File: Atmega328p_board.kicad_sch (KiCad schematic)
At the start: 25 parts, among them U1 24LC1025, U2 24LC1025, U3 ATMEGA328P-AU, U4 DS1337S_, Y1 16MHz, Y2 32.768 KHz

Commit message: Completed commits
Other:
- note added: "EEPROM"
- note added: "MCU"
- note added: "Mounting"
- note added: "RTC"
- moved on the sheet: H1, H2, H3, H4

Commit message: Routing completed.
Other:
- title: (none) -> MCU Datalogger with EEPROM and RTC
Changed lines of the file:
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@@
 (kicad_sch (version 20230121) (generator eeschema)
   (paper "A4")
+  (title_block
+    (title "MCU Datalogger with EEPROM and RTC")
+  )
   (junction (at 164.465 60.325) (diameter 0) (color 0 0 0 0)
   )

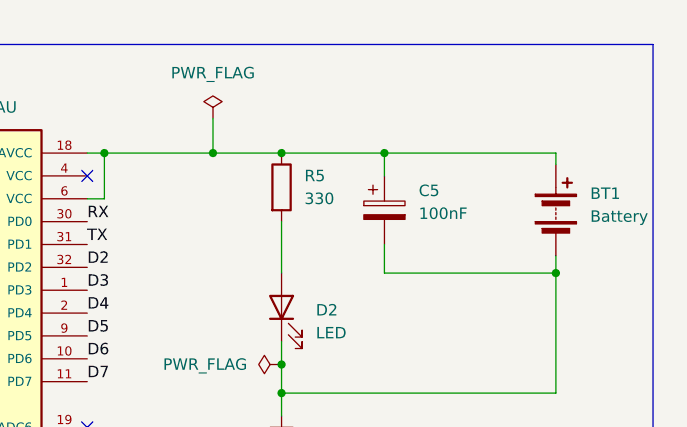
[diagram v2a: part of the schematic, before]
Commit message: COmpleted with silkscreen and footprints(logo).
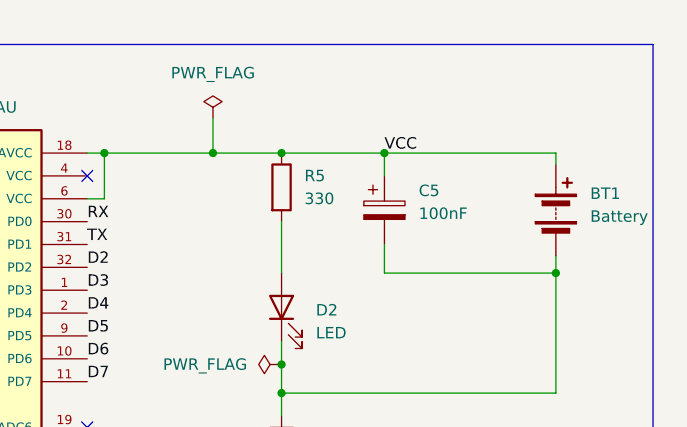
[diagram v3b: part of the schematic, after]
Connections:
- net VCC: now also BT1.1 (+), C5.1, R5.1, U3.18 (AVCC), U3.6 (VCC)
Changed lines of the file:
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@@
+    (effects (font (size 1.27 1.27)) (justify left bottom))
+  )
+  (label "VCC" (at 248.92 31.75 0) (fields_autoplaced)
     (effects (font (size 1.27 1.27)) (justify left bottom))
   )

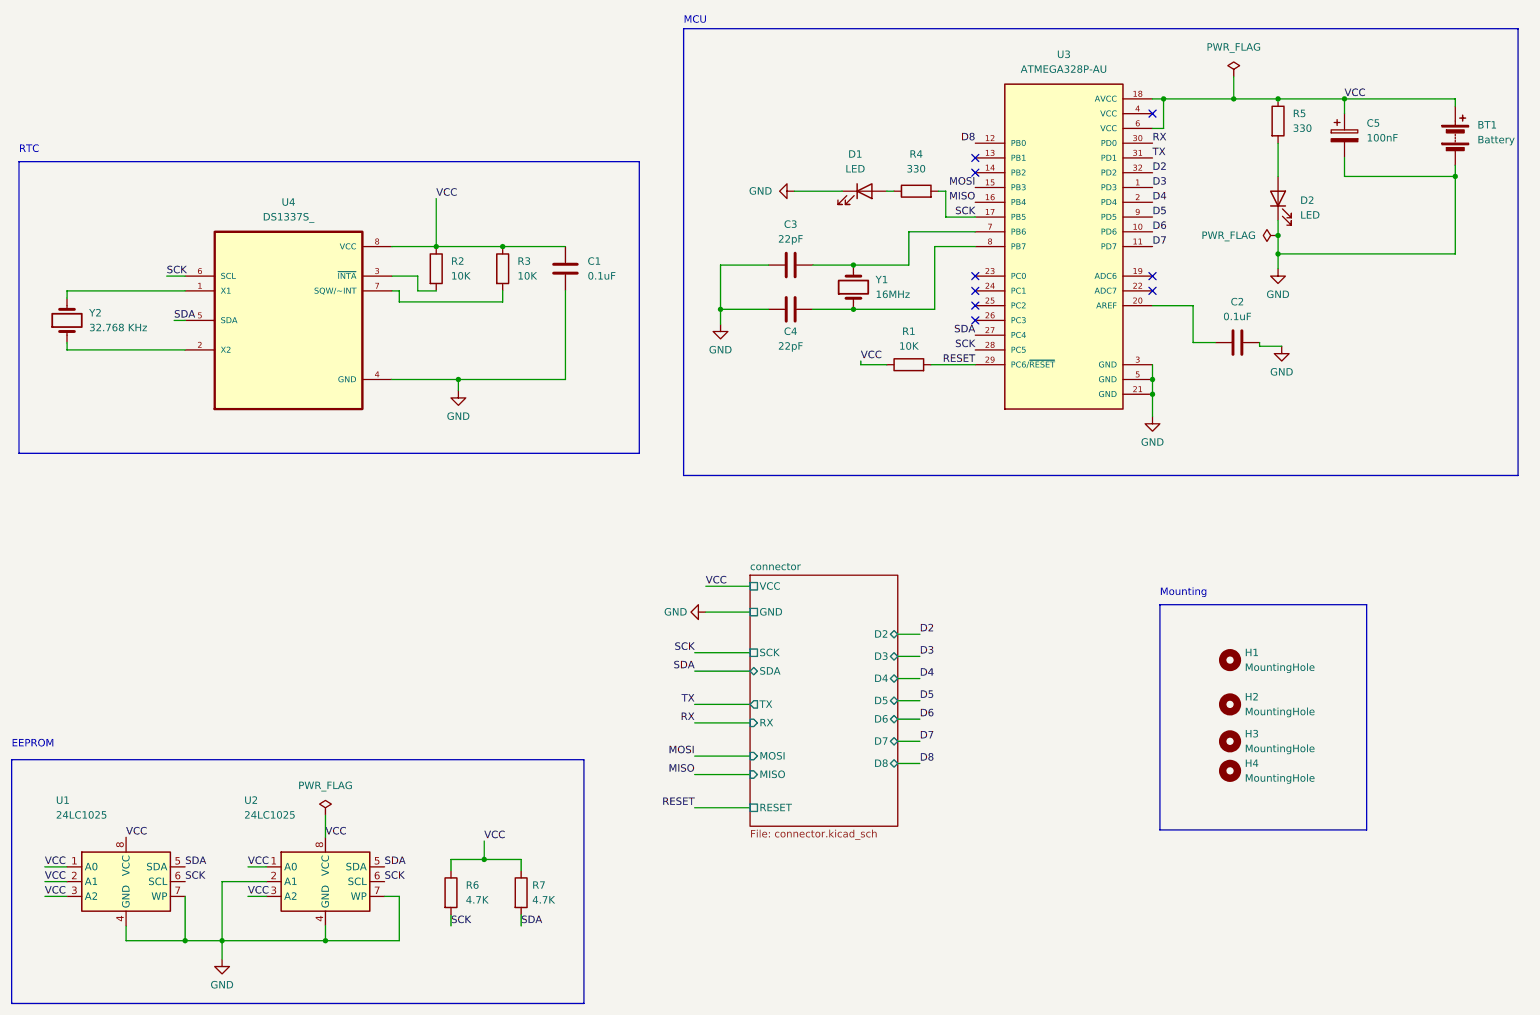
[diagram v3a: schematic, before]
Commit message: 2 detects are resolved in schematic
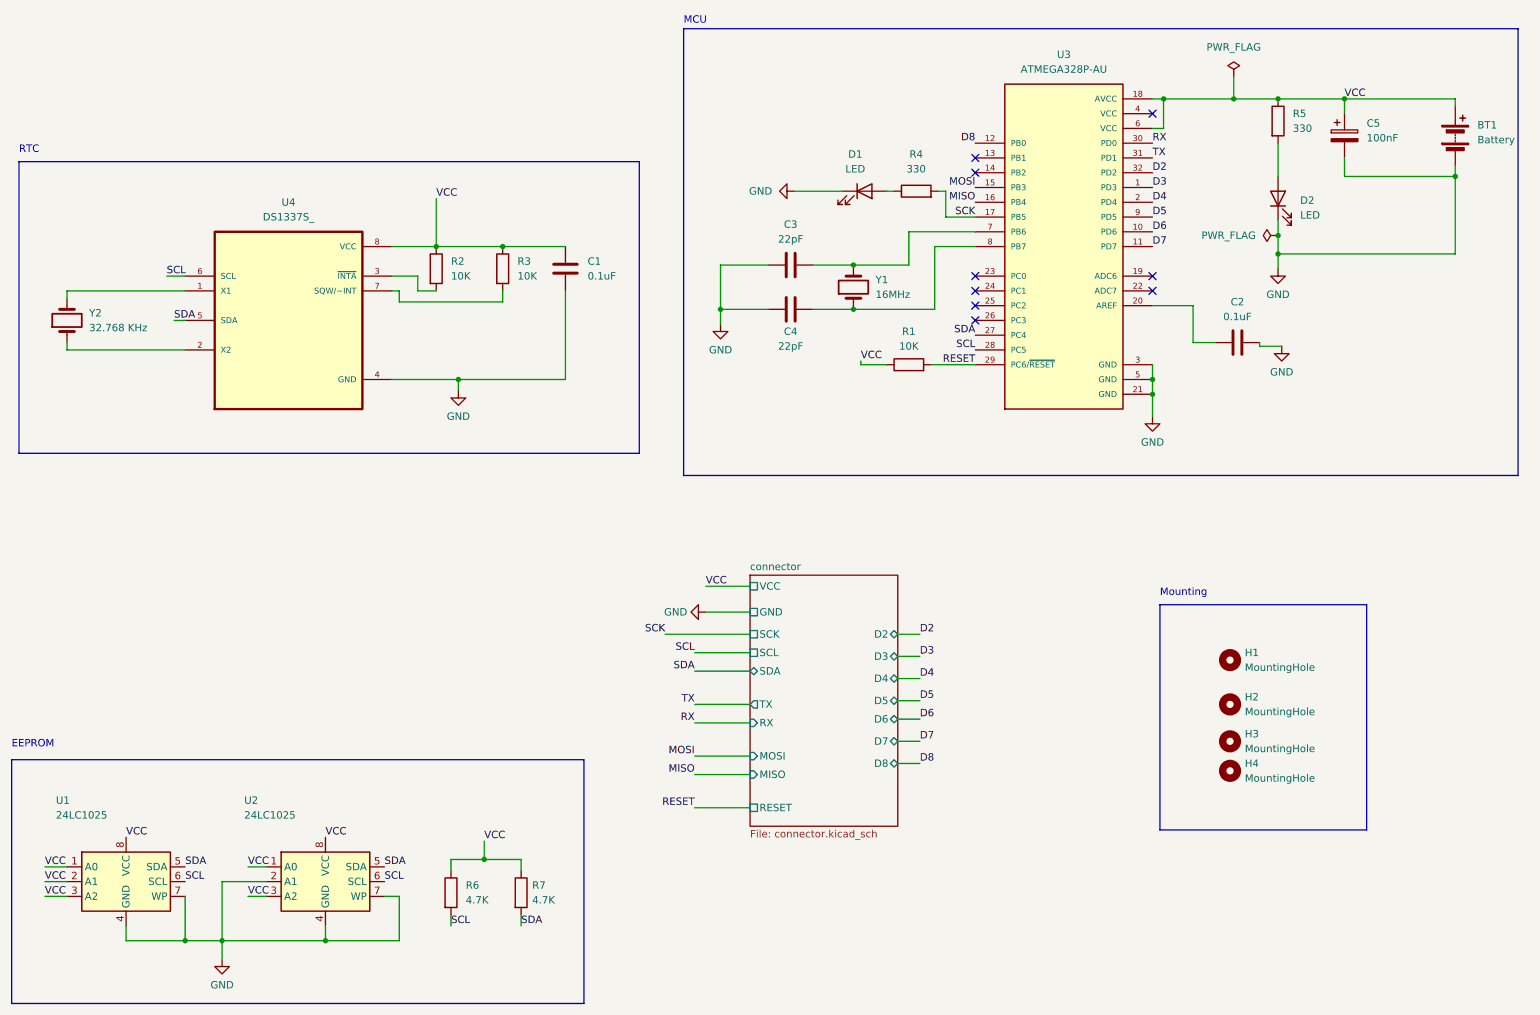
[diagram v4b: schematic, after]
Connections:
- net SCK: no longer R6.2, U1.6 (SCL), U2.6 (SCL), U3.28 (PC5), U4.6 (SCL)
- new net SCL: R6.2, U1.6 (SCL), U2.6 (SCL), U3.28 (PC5), U4.6 (SCL)
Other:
- sheet connector ports: added SCL; removed none
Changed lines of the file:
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@@
+    (stroke (width 0) (type default))
+  )
+  (wire (pts (xy 132.08 123.825) (xy 146.685 123.825))
     (stroke (width 0) (type default))
   )
@@
     (stroke (width 0) (type default))
   )
-  (wire (pts (xy 73.66 154.94) (xy 73.66 158.75))
-    (stroke (width 0) (type default))
-  )
   (polyline (pts (xy 20.955 42.545) (xy 127.635 42.545))
     (stroke (width 0) (type default))
@@
     (effects (font (size 1.27 1.27)) (justify left bottom))
   )
-  (label "SCK" (at 95.25 173.99 0) (fields_autoplaced)
+  (label "SCL" (at 95.25 173.99 0) (fields_autoplaced)
     (effects (font (size 1.27 1.27)) (justify left bottom))
   )
@@
     (effects (font (size 1.27 1.27)) (justify left bottom))
   )
-  (label "SCK" (at 83.82 166.37 0) (fields_autoplaced)
+  (label "SCL" (at 83.82 166.37 0) (fields_autoplaced)
     (effects (font (size 1.27 1.27)) (justify left bottom))
   )
@@
     (effects (font (size 1.27 1.27)) (justify left bottom))
   )
-  (label "SCK" (at 46.355 62.23 0) (fields_autoplaced)
+  (label "SCL" (at 46.355 62.23 0) (fields_autoplaced)
     (effects (font (size 1.27 1.27)) (justify left bottom))
   )
@@
     (effects (font (size 1.27 1.27)) (justify left bottom))
   )
-  (label "SCK" (at 137.16 127 180) (fields_autoplaced)
+  (label "SCL" (at 137.16 127 180) (fields_autoplaced)
     (effects (font (size 1.27 1.27)) (justify right bottom))
   )
@@
     (effects (font (size 1.27 1.27)) (justify left bottom))
   )
-  (label "SCK" (at 185.42 74.93 180) (fields_autoplaced)
+  (label "SCL" (at 185.42 74.93 180) (fields_autoplaced)
     (effects (font (size 1.27 1.27)) (justify right bottom))
   )
@@
     (effects (font (size 1.27 1.27)) (justify left bottom))
   )
-  (label "SCK" (at 49.53 166.37 0) (fields_autoplaced)
+  (label "SCL" (at 49.53 166.37 0) (fields_autoplaced)
     (effects (font (size 1.27 1.27)) (justify left bottom))
   )
@@
   (label "VCC" (at 165.735 76.835 0) (fields_autoplaced)
     (effects (font (size 1.27 1.27)) (justify left bottom))
+  )
+  (label "SCK" (at 132.08 123.825 180) (fields_autoplaced)
+    (effects (font (size 1.27 1.27)) (justify right bottom))
   )
   (label "TX" (at 215.9 41.91 0) (fields_autoplaced)
@@
     )
   )
-  (symbol (lib_id "power:PWR_FLAG") (at 73.66 154.94 0) (unit 1)
-    (in_bom yes) (on_board yes) (dnp no) (fields_autoplaced)
-    (property "Reference" "#FLG03" (at 73.66 153.035 0)
-      (effects (font (size 1.27 1.27)) hide)
-    )
-    (property "Value" "PWR_FLAG" (at 73.66 149.86 0)
-      (effects (font (size 1.27 1.27)))
-    )
-    (property "Footprint" "" (at 73.66 154.94 0)
-      (effects (font (size 1.27 1.27)) hide)
-    )
-    (property "Datasheet" "~" (at 73.66 154.94 0)
-      (effects (font (size 1.27 1.27)) hide)
-    )
-    (pin "1")
-    (instances
-      (project "Atmega328p_board"
-        (path "/95a6a7eb-84a1-437e-9a5b-5923195e1e42"
-          (reference "#FLG03") (unit 1)
-        )
-      )
-    )
-  )
   (symbol (lib_id "power:PWR_FLAG") (at 229.87 27.94 0) (unit 1)
     (in_bom yes) (on_board yes) (dnp no) (fields_autoplaced)
@@
       (effects (font (size 1.27 1.27)) (justify left))
     )
-    (pin "SCK" passive (at 146.685 127 180)
-      (effects (font (size 1.27 1.27)) (justify left))
-    )
     (pin "SDA" bidirectional (at 146.685 130.175 180)
       (effects (font (size 1.27 1.27)) (justify left))
@@
       (effects (font (size 1.27 1.27)) (justify left))
     )
+    (pin "SCL" passive (at 146.685 127 180)
+      (effects (font (size 1.27 1.27)) (justify left))
+    )
+    (pin "SCK" passive (at 146.685 123.825 180)
+      (effects (font (size 1.27 1.27)) (justify left))
+    )
